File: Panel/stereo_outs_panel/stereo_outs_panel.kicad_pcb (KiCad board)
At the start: 2 copper layers, 100 x 200 mm, 22 parts

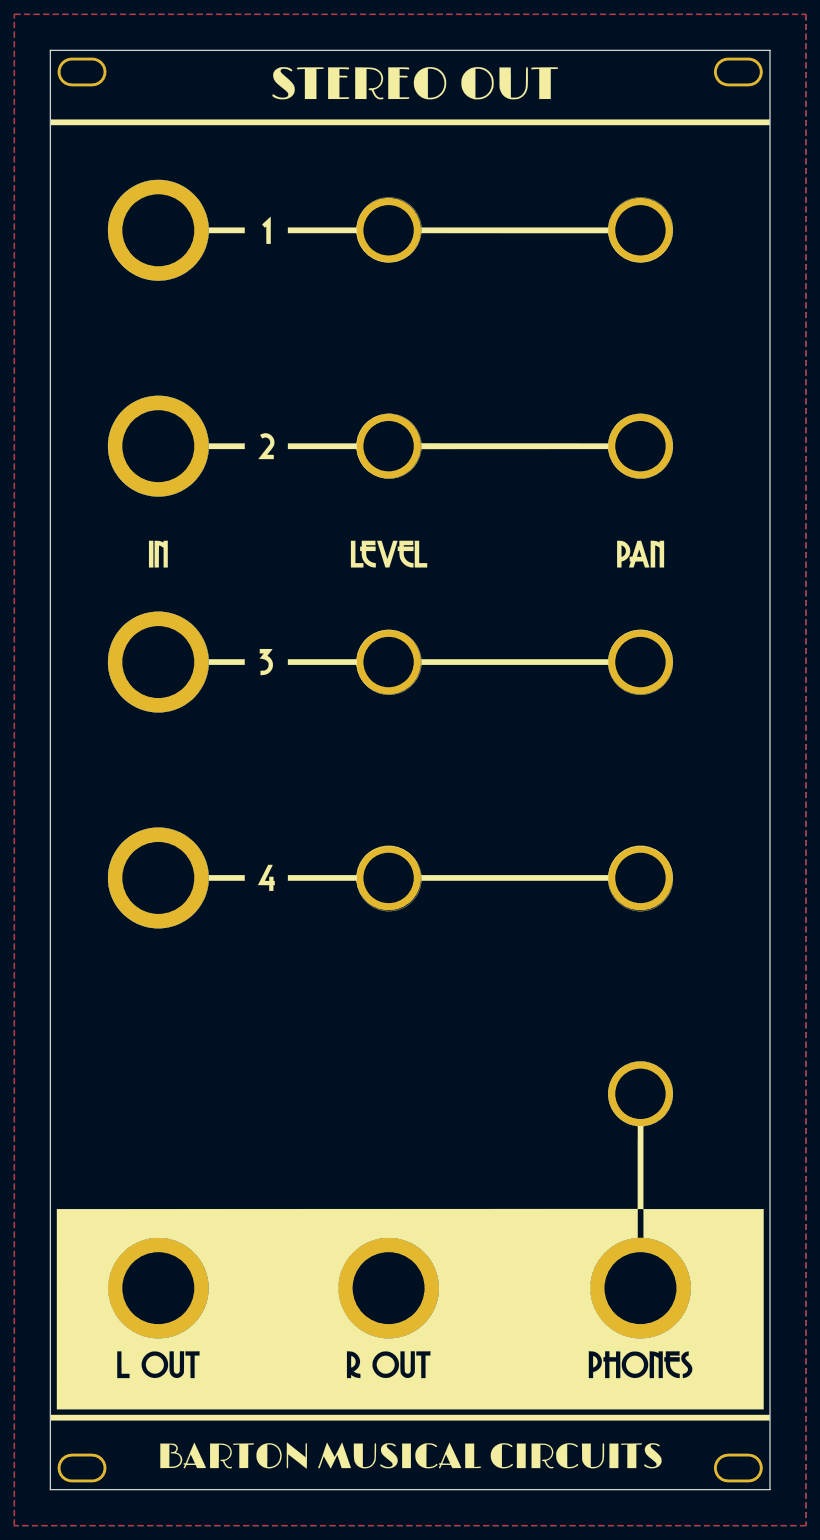
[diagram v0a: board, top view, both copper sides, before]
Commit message: Finalize design and add Gerbers for first PCB run
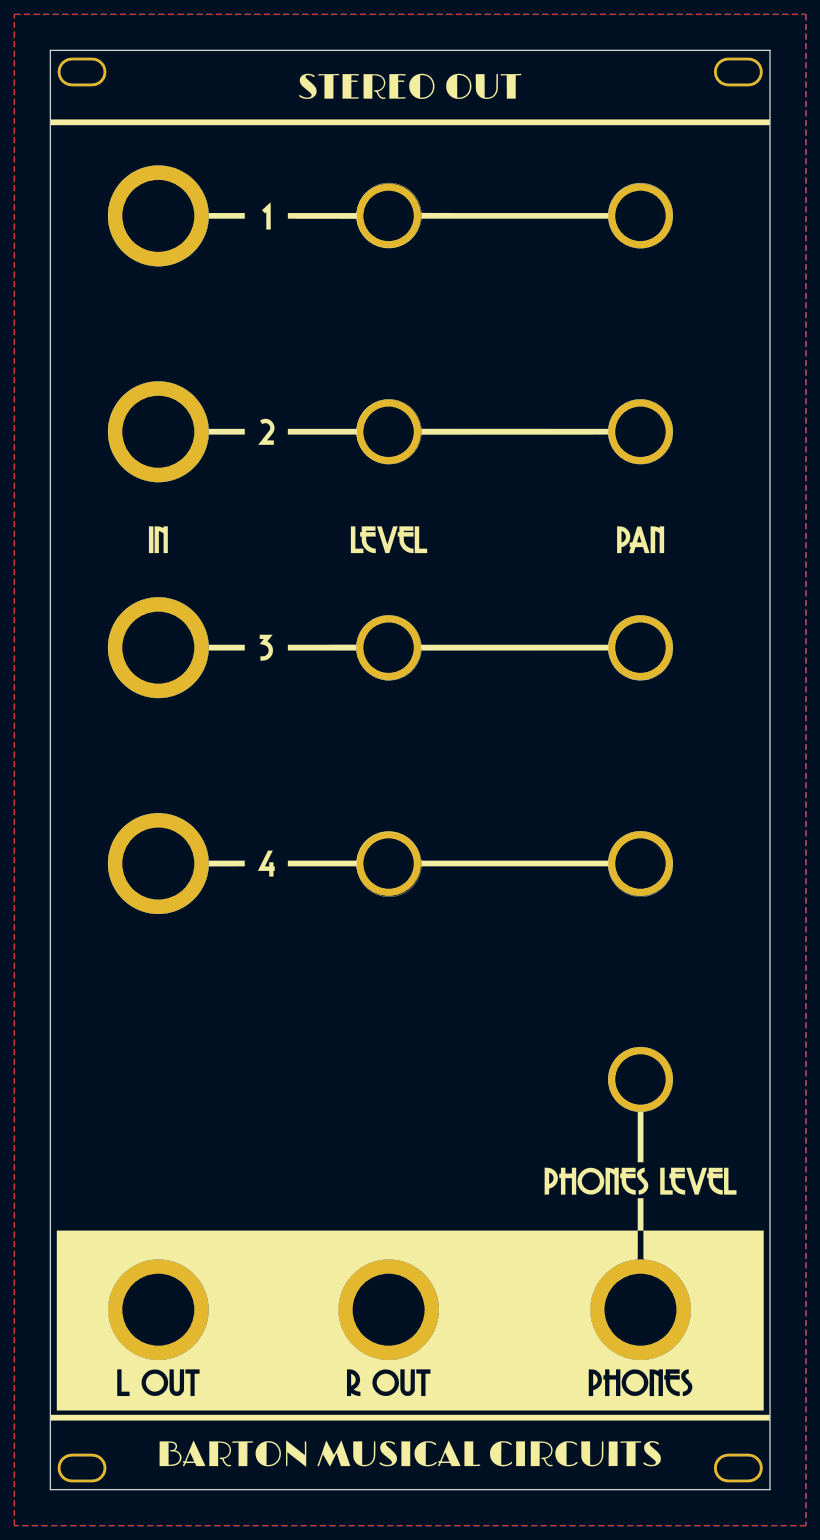
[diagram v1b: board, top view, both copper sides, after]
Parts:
- moved H5 3.00 mm to (65.0, 195.0)
- moved H6 3.00 mm to (97.0, 195.0)
- moved H7 3.00 mm to (132.0, 195.0)
- moved H1 2.00 mm to (65.0, 43.0)
- moved H10 2.00 mm to (132.0, 73.0)
- moved H11 2.00 mm to (97.0, 103.0)
- moved H12 2.00 mm to (97.0, 73.0)
- moved H13 2.00 mm to (132.0, 43.0)
- moved H14 2.00 mm to (97.0, 43.0)
- moved H15 2.00 mm to (132.0, 133.0)
- moved H16 2.00 mm to (132.0, 163.0)
- moved H2 2.00 mm to (65.0, 73.0)
- moved H3 2.00 mm to (65.0, 103.0)
- moved H4 2.00 mm to (65.0, 133.0)
- moved H8 2.00 mm to (97.0, 133.0)
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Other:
- board text added: "Panel design Rich Holmes Sep 2020"
- board text removed: "Panel design: Rich Holmes 9/2020"
